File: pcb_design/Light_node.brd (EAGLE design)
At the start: 17.8 x 37.3 mm, 44 parts, among them CN3 JSTPH, IC1 ATmega328P, IC2 MIC5225-3.3v, U1 MCP73831T-2ACI/OT, U2 LIS3DHTR, Y1 12MHz

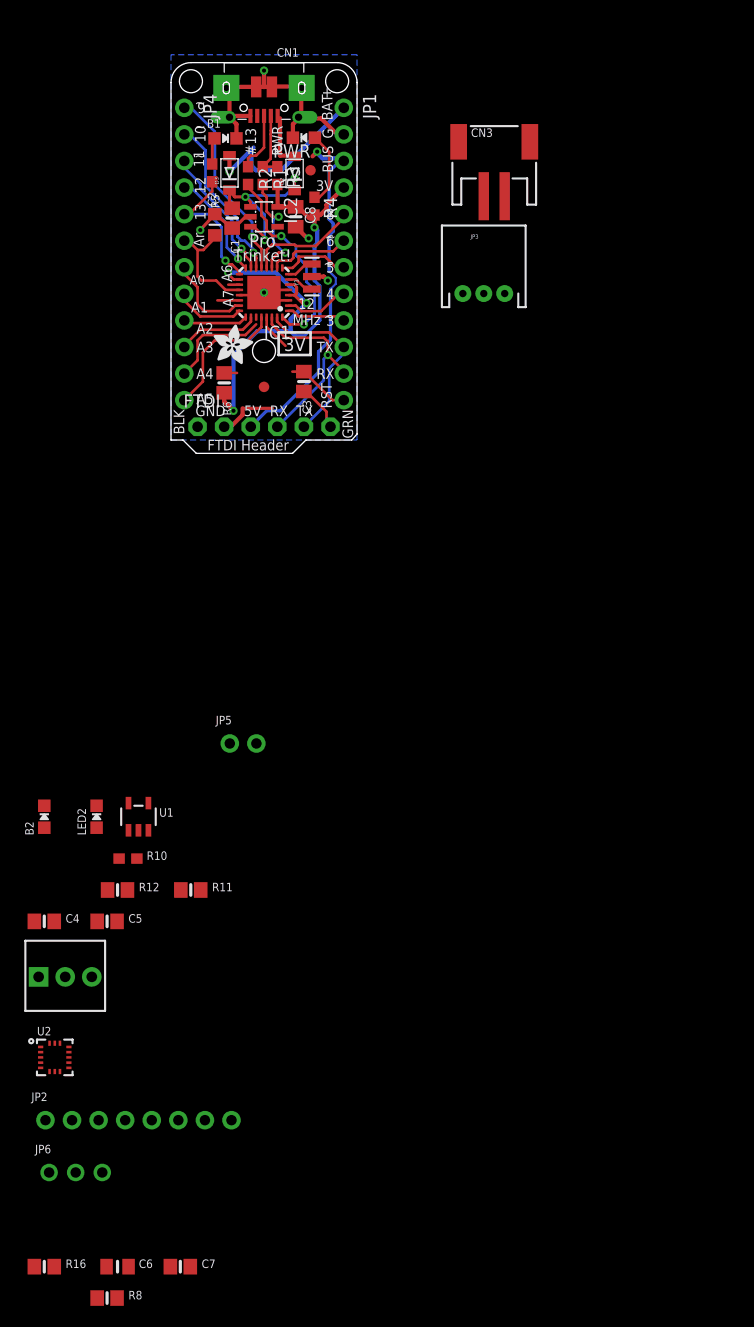
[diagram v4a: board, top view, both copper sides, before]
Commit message: most of the layour is completed using standard LEDs, but we should move to neopixels on board
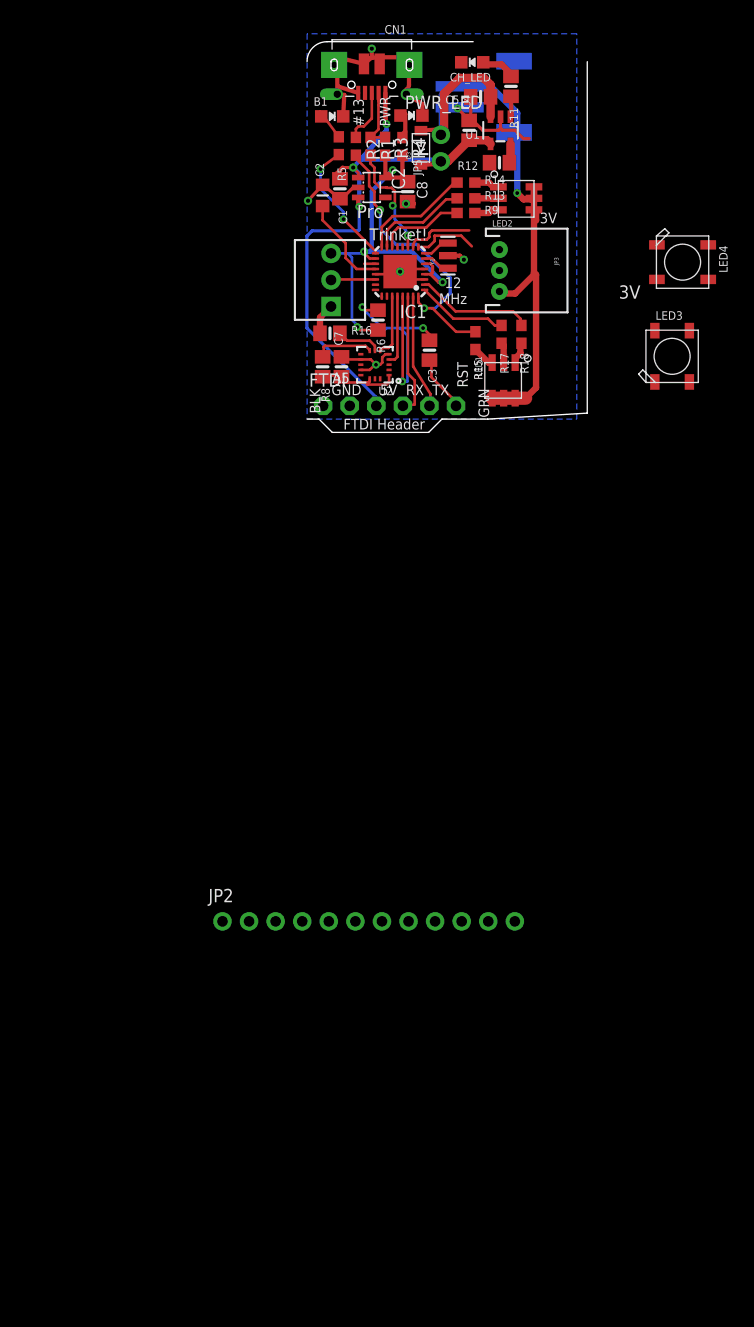
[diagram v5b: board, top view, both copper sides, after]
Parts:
- removed B2: red, microbuilder:CHIPLED_0805_NOOUTLINE
- removed C6: 0.1uF, microbuilder:0805_10MGAP
- removed D2: SCHOTTKY, adafruit:SOD-123FL
- removed JP1, JP4: (no value), adafruit:1X12-CB
- removed JP6: (no value), microbuilder:1X03_ROUND
- removed PWR: green, microbuilder:CHIPLED_0805_NOOUTLINE
- removed R10: 470 (0603), microbuilder:0603-NO
- removed U$1, U$6: FIDUCIAL, adafruit:FIDUCIAL_1MM
- removed U$7: (no value), microbuilder:ADAFRUIT_3.5MM
- removed U$9: (no value), microbuilder:ADAFRUIT_9MM
- added CH_LED: GREEN, microbuilder:CHIPLED_0805_NOOUTLINE
- added LED1: RGB_LED, 0_Shibbs1:LED_LX6
- added LED3, LED4: WS2812B5050, microbuilder:WS2812B
- added PWR_LED: green, microbuilder:CHIPLED_0805_NOOUTLINE
- added R13, R14, R15, R17, R18, R9: 470 (0603), microbuilder:0603-NO
- JP2: device microbuilder:1X08_ROUND_70 -> adafruit:1X12-CB
- LED2: value GREEN -> RGB_LED; device microbuilder:CHIPLED_0805_NOOUTLINE -> 0_Shibbs1:LED_LX6
- moved R16 93.3 mm to (6.30, 10.2)
- moved R8 91.4 mm to (5.60, 7.00), turned to 270 degrees
- moved C7 87.4 mm to (7.40, 7.00), turned to 90 degrees
- moved C5 86.5 mm to (20.7, 32.8), turned to 180 degrees
- moved C4 85.8 mm to (19.6, 29.6), turned to 90 degrees
- moved R11 82.7 mm to (23.6, 33.8), turned to 270 degrees
- moved R12 78.5 mm to (22.5, 26.5), turned to 180 degrees
- moved U1 74.2 mm to (22.6, 29.6), turned to 180 degrees
- moved U2 72.9 mm to (10.6, 7.20), turned to 180 degrees
- moved LED2 71.4 mm to (24.1, 23.1)
- moved R7 70.9 mm to (6.10, 15.3), turned to 90 degrees
- moved JP5 60.0 mm to (16.9, 27.9), turned to 90 degrees
- moved JP2 29.1 mm to (10.0, -46.0)
- moved D3 18.5 mm to (15.0, 27.9)
- moved R6 15.9 mm to (10.9, 11.5)
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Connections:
- removed net VBUS: FTDI.3, JP1.3
- removed net VIN: JP2.1
- new net +5V1: LED3.1-VDD, LED4.1-VDD
- new net GND1: LED3.3-GND, LED4.3-GND
- new net LED_CNTRL: LED3.4-DIN
- new net N$10: LED2.P1, R14.2
- new net N$11: LED1.P3, R15.2
- new net N$12: LED1.P2, R17.2
- new net N$13: LED1.P1, R18.2
- new net N$14: LED2.P3, R9.2
- new net N$15: LED4.2-DOUT
- net +3V3: no longer JP1.4
- net +5V: now also C1.1, D3.C, FTDI.3, IC2.1, IC2.3; no longer D2.A, R10.2
- net 3.3V: no longer C6.1, JP2.2
- net A0: no longer JP4.7
- net A1: no longer JP4.8
- net A2: no longer JP4.9
- net A3: no longer JP4.10
- net A6: no longer R7.2
- net A7: now also R7.2
- net ADC1: no longer JP6.1
- net ADC2: no longer JP6.2
- net ADC3: no longer JP6.3
- net AREF: no longer JP4.6
- net CS: no longer JP2.7
- net D10: now also R9.1; no longer JP4.2
- net D11: now also R13.1; no longer JP4.3
- net D12: now also R14.1; no longer JP4.4
- net D13: no longer JP4.5
- net D2: now also R15.1
- net D3: now also R17.1; no longer JP1.9
- net D4: now also R18.1; no longer JP1.8
- net D5: no longer JP1.7
- net D6: no longer JP1.6
- net D8: no longer JP1.5
- net D9: no longer JP4.1
- net GND: now also CH_LED.C, PWR_LED.C; no longer B2.C, C6.2, JP1.2, JP2.3, LED2.C, PWR.C
- net INT1: no longer JP2.8
- net N$4: now also LED3.2-DOUT, LED4.4-DIN; no longer B2.A, R10.1
- net N$6: now also PWR_LED.A; no longer PWR.A
- net N$7: now also LED2.P2, R13.2; no longer C1.1, D2.C, D3.C, IC2.1, IC2.3
- net N$9: now also CH_LED.A; no longer LED2.A
- net RESET: no longer JP1.12
- net RXD: no longer JP1.11
- net SCL: no longer JP2.4, JP4.12
- net SDA: no longer JP2.5, JP4.11
- net SDO: no longer JP2.6
- net TXD: no longer JP1.10
- net VBAT: now also LED1.P4, LED1.P5, LED1.P6, LED2.P4, LED2.P5, LED2.P6; no longer JP1.1
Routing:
- net +5V: track 5.00 -> 62.5 mm, vias 0 -> 3
- net VBAT: track 17.8 -> 69.8 mm
- net VBUS: track 34.5 -> 0.00 mm, vias 1 -> 0
- net D9: track 18.7 -> 0.00 mm, vias 1 -> 0
- net N$7: track 19.6 -> 2.25 mm, vias 3 -> 0
- net GND: track 49.5 -> 65.3 mm, vias 5 -> 7
- net RESET: track 10.8 -> 23.9 mm, vias 0 -> 3
- net +3V3: track 55.7 -> 43.0 mm
- net D8: track 10.8 -> 0.00 mm
- net D2: track 20.0 -> 29.8 mm
- net A0: track 8.56 -> 0.00 mm
- net 3.3V: track 0.00 -> 8.20 mm
- net A3: track 7.88 -> 0.00 mm
- net D10: track 16.1 -> 8.31 mm, vias 1 -> 0
- net RXD: track 19.3 -> 11.8 mm, vias 1 -> 0
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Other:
- board size 17.8 x 37.3 mm -> 26.8 x 37.3 mm
- board text removed: "+"
- board text removed: "10"
- board text removed: "11"
- board text removed: "12"
- board text removed: "13"
- board text removed: "3"
- board text removed: "4"
- board text removed: "5"
- board text removed: "6"
- board text removed: "8"
- board text removed: "9"
- board text removed: "A0"
- board text removed: "A1"
- board text removed: "A2"
- board text removed: "A3"
- board text removed: "A4"
- board text removed: "A6"
- board text removed: "A7"
- board text removed: "Adafruit Pro Trinket ATmega328p 3V / 12MHz"
- board text removed: "Ar"
- board text removed: "BAT"
- board text removed: "BUS"
- board text removed: "G"
- board text removed: "VBat JST"
- board text removed: "VBat: 3.5-16VDC"
- board text removed: "~"

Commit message: moved us to neopixels, added breakout headers, almost done
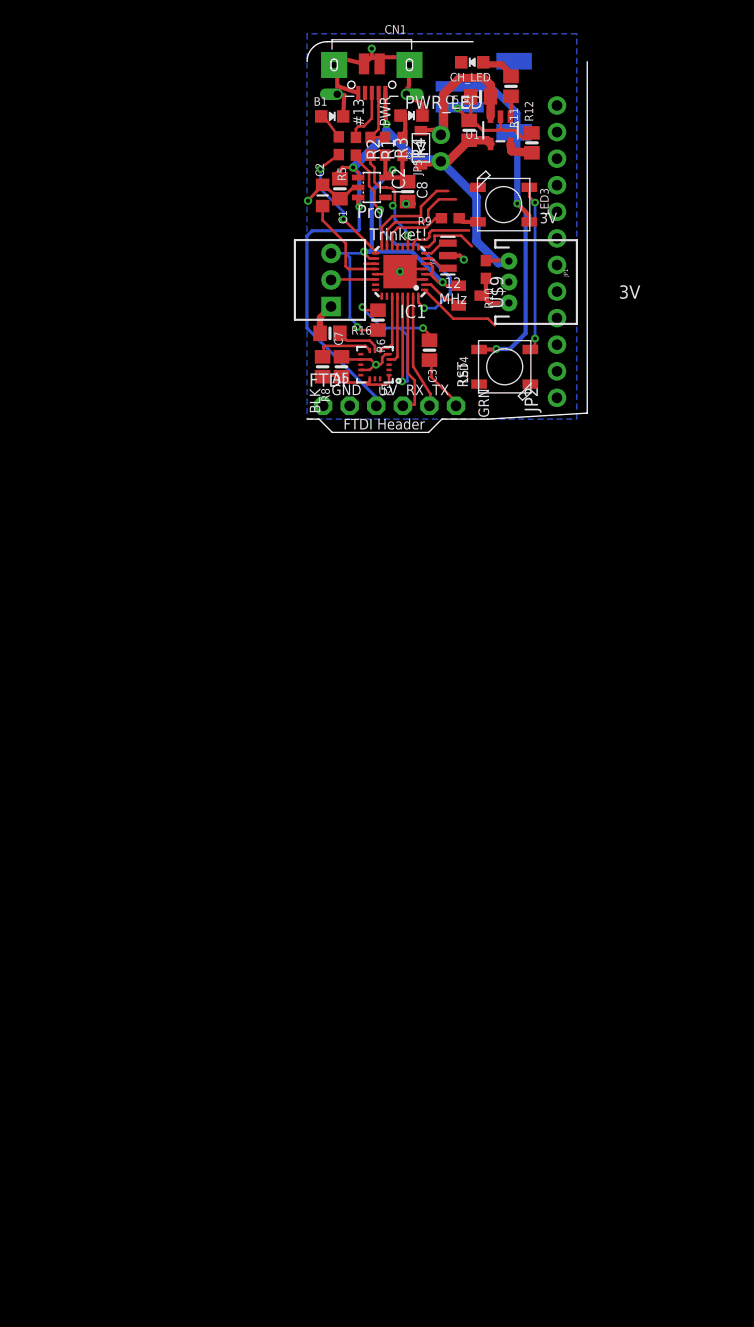
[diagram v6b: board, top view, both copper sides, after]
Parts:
- removed JP3: (no value), SparkFun:JST-3-PTH
- removed LED1, LED2: RGB_LED, 0_Shibbs1:LED_LX6
- removed R13, R14, R15, R17, R18: 470 (0603), microbuilder:0603-NO
- added JP1: (no value), SparkFun:JST-3-PTH
- added R10: 10K, microbuilder:0603-NO
- added U$9: COMMON_ANODE_DIODE, 0_AlpineLabs:SOT23
- R9: value 470 (0603) -> 100
- moved JP2 66.5 mm to (28.0, 18.0), turned to 90 degrees
- moved LED3 21.7 mm to (22.9, 22.5), turned to 0 degrees
- moved LED4 19.7 mm to (23.0, 7.00), turned to 180 degrees
- moved R12 3.64 mm to (25.6, 28.4), turned to 90 degrees
- moved R9 1.58 mm to (17.8, 21.2), turned to 180 degrees
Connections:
- removed net +5V1: LED3.1-VDD, LED4.1-VDD
- removed net GND1: LED3.3-GND, LED4.3-GND
- removed net N$10: LED2.P1, R14.2
- removed net N$11: LED1.P3, R15.2
- removed net N$12: LED1.P2, R17.2
- removed net N$13: LED1.P1, R18.2
- removed net N$14: LED2.P3, R9.2
- removed net N$7: LED2.P2, R13.2
- net +3V3: now also U$9.1
- net +5V: now also JP1.1, R10.1
- net D10: now also R9.2; no longer R9.1
- net D11: no longer R13.1
- net D12: no longer R14.1
- net D2: no longer R15.1
- net D3: no longer R17.1
- net D4: now also U$9.2; no longer R18.1
- net GND: now also JP1.2, LED3.3-GND, LED4.3-GND; no longer JP3.1
- net LED_CNTRL: now also R9.1
- net STRIP_CNTRL: now also JP1.3, R10.2, U$9.3; no longer JP3.2
- net VBAT: now also LED3.1-VDD, LED4.1-VDD; no longer JP3.3, LED1.P4, LED1.P5, LED1.P6, LED2.P4, LED2.P5, LED2.P6
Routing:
- net N$4: track 0.00 -> 15.9 mm, vias 0 -> 2
- net VBAT: track 69.8 -> 57.6 mm, vias 1 -> 2
- net +5V: track 62.5 -> 72.9 mm
- net D4: track 11.2 -> 4.08 mm
- net D2: track 29.8 -> 24.0 mm
- net STRIP_CNTRL: track 0.00 -> 4.71 mm
- net N$10: track 2.42 -> 0.00 mm
- net N$14: track 2.37 -> 0.00 mm
- net N$7: track 2.25 -> 0.00 mm
- net N$11: track 2.12 -> 0.00 mm
- net N$13: track 2.10 -> 0.00 mm
- net LED_CNTRL: track 0.00 -> 1.94 mm
- net N$12: track 1.93 -> 0.00 mm
- net +3V3: track 43.0 -> 44.7 mm
- net D10: track 8.31 -> 6.60 mm
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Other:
- board text removed: "-"

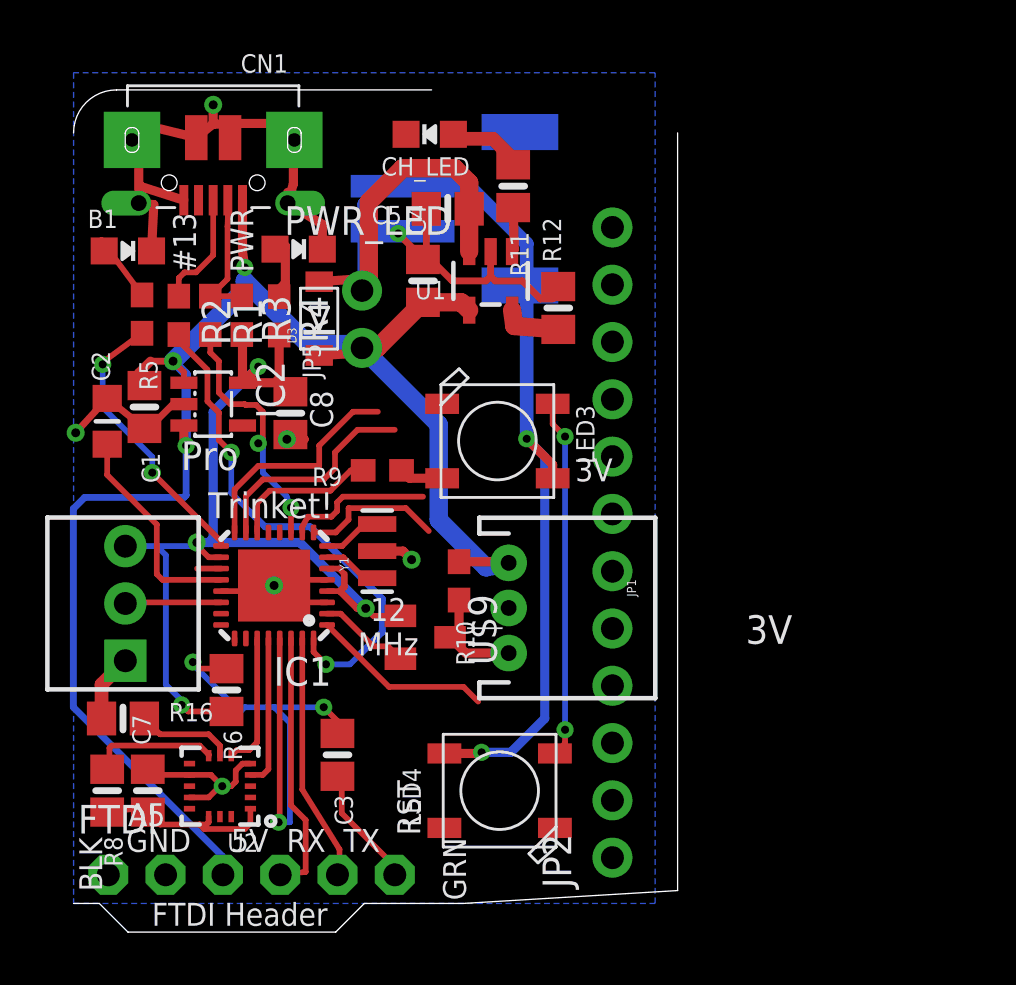
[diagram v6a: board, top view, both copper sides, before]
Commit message: moced some parts around
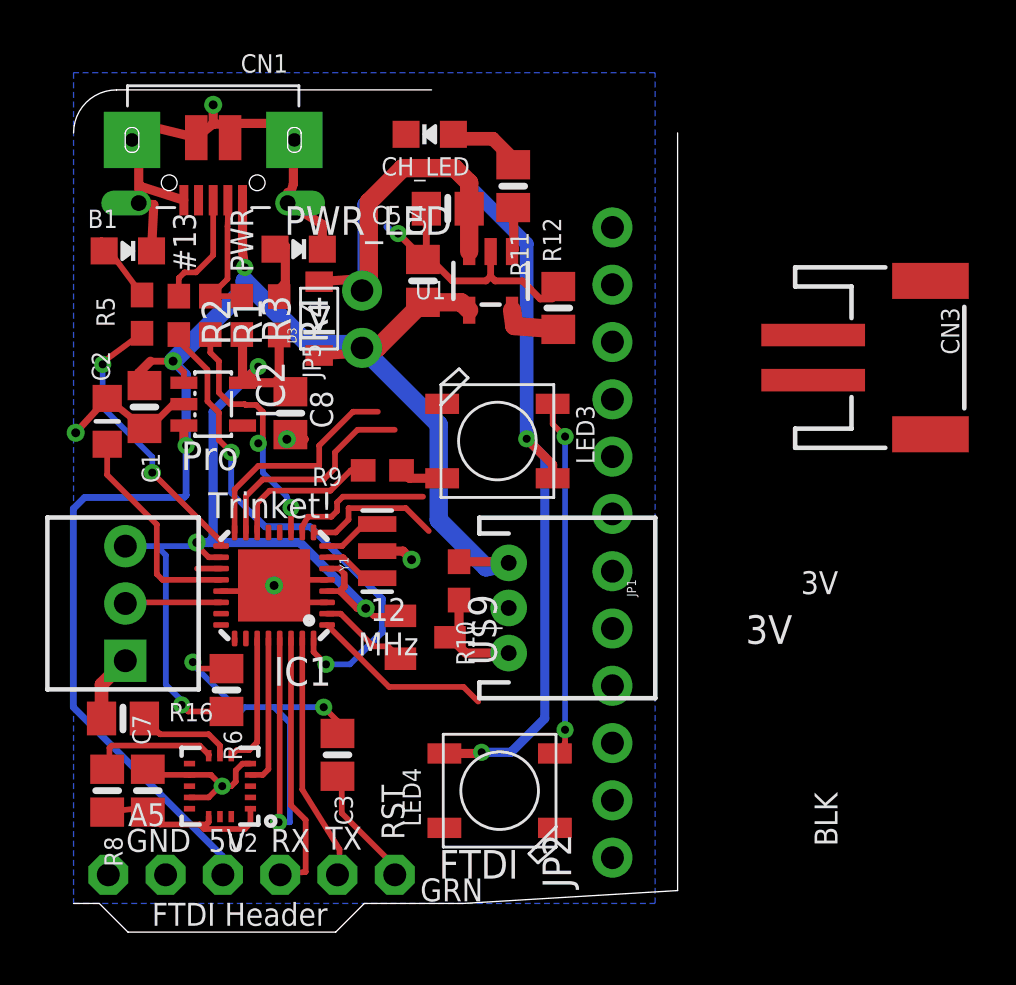
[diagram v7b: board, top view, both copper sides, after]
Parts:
- moved CN3 19.4 mm to (40.6, 26.2), flipped to the top, turned to 270 degrees
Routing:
- net VBAT: track 57.6 -> 53.6 mm
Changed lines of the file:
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@@
 <setting verticaltext="up"/>
 </settings>
-<grid distance="1" unitdist="mm" unit="mm" style="lines" multiple="1" display="yes" altdistance="0.1" altunitdist="mm" altunit="mm"/>
+<grid distance="0.0393700787" unitdist="inch" unit="inch" style="lines" multiple="1" display="yes" altdistance="0.1" altunitdist="mm" altunit="mm"/>
 <layers>
 <layer number="1" name="Top" color="4" fill="1" visible="yes" active="yes"/>
@@
 <wire x1="17.0005" y1="2" x2="21.382" y2="2" width="0" layer="20"/>
 <wire x1="21.382" y1="2" x2="30.89" y2="2.5715" width="0" layer="20"/>
-<text x="26.353" y="21.2205" size="1.016" layer="21" font="vector" ratio="10" rot="R180" align="center-right">3V</text>
-<text x="4.872" y="4.921" size="1.016" layer="21" font="vector" ratio="10" rot="R90" align="center-right">BLK</text>
-<text x="21.001" y="4.921" size="1.016" layer="21" font="vector" ratio="10" rot="R90" align="center-right">GRN</text>
-<text x="18.969" y="7.461" size="1.016" layer="21" font="vector" ratio="10" rot="R90" align="center-right">RST</text>
-<text x="17.699" y="4.794" size="1.016" layer="21" font="vector" ratio="10" align="center-right">TX</text>
-<text x="15.286" y="4.794" size="1.016" layer="21" font="vector" ratio="10" align="center-right">RX</text>
-<text x="12.746" y="4.794" size="1.016" layer="21" font="vector" ratio="10" align="center-right">5V</text>
+<text x="36.353" y="16.2205" size="1.016" layer="21" font="vector" ratio="10" rot="R180" align="center-right">3V</text>
+<text x="37.472" y="6.921" size="1.016" layer="21" font="vector" ratio="10" rot="R90" align="center-right">BLK</text>
+<text x="19.479" y="2.601" size="1.016" layer="21" font="vector" ratio="10" rot="R180" align="center-right">GRN</text>
+<text x="18.269" y="7.261" size="1.016" layer="21" font="vector" ratio="10" rot="R90" align="center-right">RST</text>
+<text x="16.899" y="4.894" size="1.016" layer="21" font="vector" ratio="10" align="center-right">TX</text>
+<text x="14.586" y="4.794" size="1.016" layer="21" font="vector" ratio="10" align="center-right">RX</text>
+<text x="11.746" y="4.794" size="1.016" layer="21" font="vector" ratio="10" align="center-right">5V</text>
 <text x="9.317" y="4.794" size="1.016" layer="21" font="vector" ratio="10" align="center-right">GND</text>
 <text x="6.523" y="5.937" size="1.016" layer="21" font="vector" ratio="10" rot="R180" align="center-right">A5</text>
@@
 </element>
 <element name="R5" library="microbuilder" package="0603-NO" value="470 (0603)" x="7.147" y="28.127" smashed="yes" rot="R270">
-<attribute name="NAME" x="7.02" y="26.095" size="0.8128" layer="25" ratio="18" rot="R270"/>
+<attribute name="NAME" x="5.12" y="28.895" size="0.8128" layer="25" ratio="18" rot="R270"/>
 <attribute name="VALUE" x="-1.616" y="33.715" size="1.016" layer="27" font="vector" ratio="10" rot="R270"/>
 </element>
@@
 </element>
 <element name="FTDI" library="adafruit" package="1X06-CLEANBIG" value="" x="12" y="3.27" smashed="yes">
-<attribute name="NAME" x="4.3038" y="5.0988" size="1.27" layer="25" ratio="10"/>
+<attribute name="NAME" x="20.3038" y="3.0988" size="1.27" layer="25" ratio="10"/>
 <attribute name="VALUE" x="4.38" y="0.095" size="1.27" layer="27"/>
 </element>
@@
 <element name="CH_LED" library="microbuilder" package="CHIPLED_0805_NOOUTLINE" value="GREEN" x="19.9" y="36.1" rot="R90"/>
 <element name="R11" library="microbuilder" package="0805-NO" value="470" x="23.6" y="33.8" rot="R270"/>
-<element name="CN3" library="microbuilder" package="JSTPH2" value="JSTPH" x="22.4" y="32.8" rot="MR90"/>
+<element name="CN3" library="microbuilder" package="JSTPH2" value="JSTPH" x="40.6" y="26.2" rot="R270"/>
 <element name="C4" library="microbuilder" package="0805-NO" value="10µF" x="19.6" y="29.6" rot="R90"/>
 <element name="C5" library="microbuilder" package="0805-NO" value="10µF" x="20.7" y="32.8" rot="R180"/>
@@
 <contactref element="JP1" pad="2"/>
 <wire x1="25.35" y1="28.8" x2="25.6" y2="29.35" width="0" layer="19" extent="1-1"/>
-<wire x1="18.7" y1="31.8" x2="18.5" y2="31.7" width="0" layer="19" extent="1-16"/>
+<wire x1="36.9" y1="27.2" x2="18.5" y2="31.7" width="0" layer="19" extent="1-16"/>
 <wire x1="15.14" y1="32.11" x2="18" y2="32" width="0" layer="19" extent="1-16"/>
 <wire x1="6.7" y1="35.85" x2="7" y2="36.199" width="0" layer="19" extent="1-1"/>
@@
 <wire x1="17.2" y1="33.1" x2="17.2" y2="29.47" width="0.8128" layer="1"/>
 <wire x1="17.2" y1="29.47" x2="16.9" y2="29.17" width="0.8128" layer="1"/>
-<wire x1="18.7" y1="33.8" x2="17.7" y2="33.7" width="0.6096" layer="16"/>
+<wire x1="36.9" y1="25.2" x2="17.7" y2="33.7" width="0" layer="19" extent="1-16"/>
 <wire x1="17.7" y1="33.7" x2="17" y2="33" width="0.6096" layer="16"/>
 <wire x1="17" y1="33" x2="17" y2="29.27" width="0.6096" layer="16"/>
@@
 <wire x1="24.2" y1="22.6" x2="24.2" y2="31.25" width="0.6096" layer="16"/>
 <wire x1="24.2" y1="31.25" x2="21.65" y2="33.8" width="0.6096" layer="16"/>
-<wire x1="21.65" y1="33.8" x2="18.7" y2="33.8" width="0.6096" layer="16"/>
+<wire x1="21.65" y1="33.8" x2="36.9" y2="25.2" width="0" layer="19" extent="1-16"/>
 <contactref element="LED3" pad="1-VDD"/>
 <contactref element="LED4" pad="1-VDD"/>
